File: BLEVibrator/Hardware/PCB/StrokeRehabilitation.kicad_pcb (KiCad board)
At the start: 2 copper layers, 32 x 48 mm, 26 parts, among them CON1 USB-MICRO-B, P2 Programming Header, Q1 MOS_P, Q2 MOSFET_N, SW1 SWITCH_INV, U1 MCP73833, U2 TPS73701_DRV_6, U3 RFD22301, U4 Brushed_DC_motor

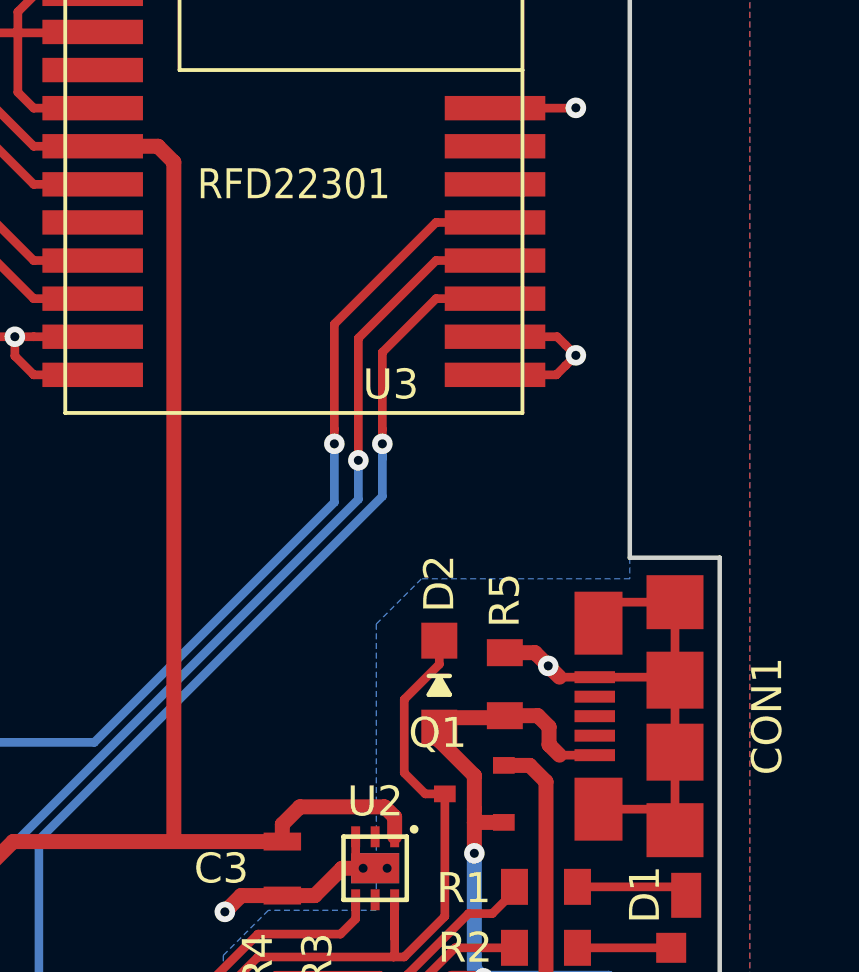
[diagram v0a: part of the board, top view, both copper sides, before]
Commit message: Place and route of LiPo voltage monitoring circuit
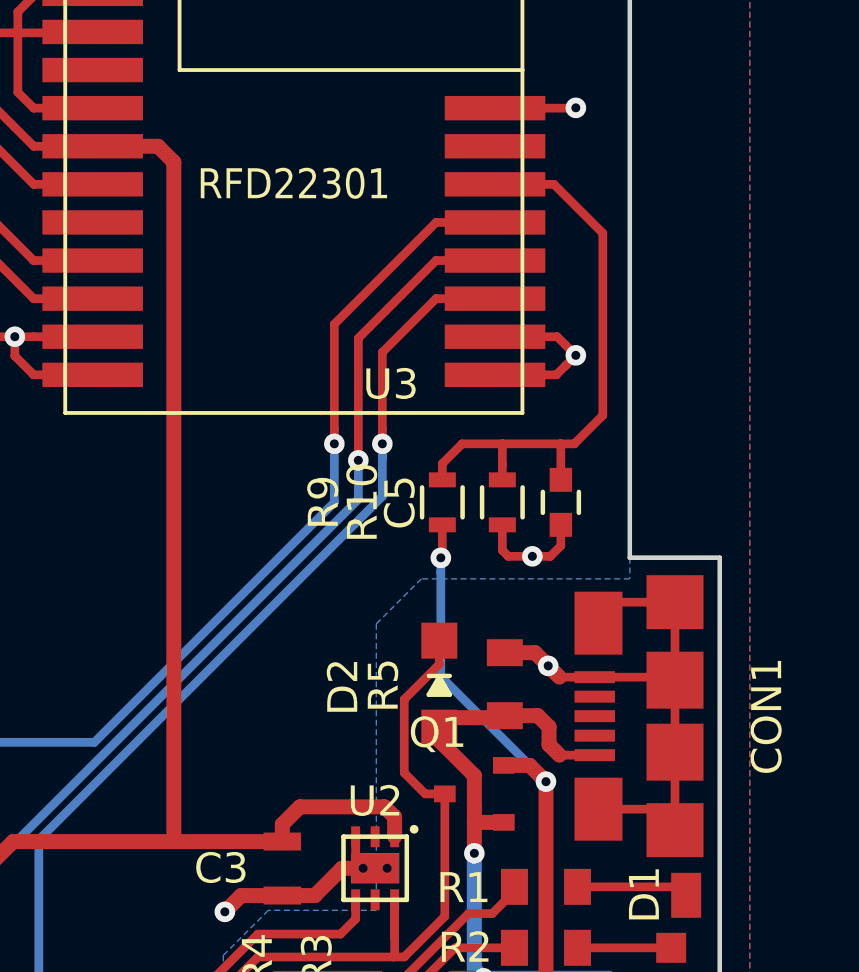
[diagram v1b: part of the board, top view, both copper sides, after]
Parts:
- added C5: 100n, Capacitors_SMD:C_0603, F.Cu at (164.2, 119.9)
- added R10: 2.2M, Resistors_SMD:R_0603, F.Cu at (162.3, 119.9)
- added R9: 10M, Resistors_SMD:R_0603, F.Cu at (160.3, 119.9)
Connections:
- U3 pad P$6: Net-(U3-PadP$6) -> BatteryLevel
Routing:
- net BatteryLevel: track 0.00 -> 19.3 mm
- net +BATT: track 21.6 -> 31.6 mm, vias 0 -> 2
- net GND: track 77.4 -> 81.1 mm, vias 8 -> 9

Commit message: Adding a test point for FACTORY pin of the RFDuino, in case SWD programming is needed in the future
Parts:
- added P1: CONN_01X01, IainPersonalLibrary:TestPoint_SMD_1x1, F.Cu at (140.8, 107.6)
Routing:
- net Net-(P1-Pad1): track 0.00 -> 11.9 mm, vias 0 -> 2
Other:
- net class Default: via_drill 0.3 -> 0.3302
- net class HighCurrent: via_drill 0.3 -> 0.3302
- net class Minimum: via_dia 0.508 -> 0.6858; via_drill 0.3 -> 0.3302
- net class Small: via_drill 0.3 -> 0.3302
- rule via_min_drill: 0.3 -> 0.3302
- rule via_min_size: 0.508 -> 0.6858
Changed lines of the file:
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@@
 (kicad_pcb (version 4) (host pcbnew 4.0.1-stable)
   (general
-    (links 85)
+    (links 86)
     (no_connects 0)
     (area 137.474999 99.424999 169.620601 147.575001)
     (thickness 0.800001)
     (drawings 22)
-    (tracks 293)
+    (tracks 300)
     (zones 0)
-    (modules 29)
+    (modules 30)
     (nets 32)
   )
@@
     (edge_width 0.15)
     (via_size 0.6858)
-    (via_drill 0.3)
-    (via_min_size 0.508)
-    (via_min_drill 0.3)
-    (user_via 0.508 0.3302)
+    (via_drill 0.3302)
+    (via_min_size 0.6858)
+    (via_min_drill 0.3302)
+    (user_via 0.6858 0.3302)
     (uvia_size 0.762)
     (uvia_drill 0.508)
@@
     (pad_drill 0.8)
     (pad_to_mask_clearance 0.2)
-    (aux_axis_origin 128.55 147.5)
-    (grid_origin 128.55 147.5)
+    (aux_axis_origin 137.55 147.5)
+    (grid_origin 137.55 147.5)
     (visible_elements 7FFFFF7F)
     (pcbplotparams
@@
   (net 28 "Net-(U3-PadP$7)")
   (net 29 "Net-(U3-PadP$11)")
-  (net 30 "Net-(U3-PadP$15)")
-  (net 31 BatteryLevel)
+  (net 30 BatteryLevel)
+  (net 31 "Net-(P1-Pad1)")
   (net_class Default "This is the default net class."
     (clearance 0.2)
     (trace_width 0.29)
     (via_dia 0.6858)
-    (via_drill 0.3)
+    (via_drill 0.3302)
     (uvia_dia 0.762)
     (uvia_drill 0.508)
@@
     (add_net "Net-(D3-Pad2)")
     (add_net "Net-(D3-Pad3)")
+    (add_net "Net-(P1-Pad1)")
     (add_net "Net-(P2-Pad2)")
     (add_net "Net-(P2-Pad3)")
@@
     (add_net "Net-(U2-Pad5)")
     (add_net "Net-(U3-PadP$11)")
-    (add_net "Net-(U3-PadP$15)")
     (add_net "Net-(U3-PadP$7)")
     (add_net VDD)
@@
     (trace_width 0.5)
     (via_dia 0.6858)
-    (via_drill 0.3)
+    (via_drill 0.3302)
     (uvia_dia 0.762)
     (uvia_drill 0.508)
@@
     (clearance 0.1524)
     (trace_width 0.1524)
-    (via_dia 0.508)
-    (via_drill 0.3)
+    (via_dia 0.6858)
+    (via_drill 0.3302)
     (uvia_dia 0.762)
     (uvia_drill 0.508)
@@
     (trace_width 0.29)
     (via_dia 0.6858)
-    (via_drill 0.3)
+    (via_drill 0.3302)
     (uvia_dia 0.762)
     (uvia_drill 0.508)
@@
       (net 3 motor) (solder_mask_margin 0.2))
     (pad P$6 smd rect (at -6.7056 0 180) (size 3.3528 0.8128) (layers F.Cu F.Paste F.Mask)
-      (net 31 BatteryLevel) (solder_mask_margin 0.2))
+      (net 30 BatteryLevel) (solder_mask_margin 0.2))
     (pad P$7 smd rect (at -6.7056 1.27 180) (size 3.3528 0.8128) (layers F.Cu F.Paste F.Mask)
       (net 28 "Net-(U3-PadP$7)") (solder_mask_margin 0.2))
@@
       (net 9 "Net-(P2-Pad2)") (solder_mask_margin 0.2))
     (pad P$15 smd rect (at 6.7056 -1.27 180) (size 3.3528 0.8128) (layers F.Cu F.Paste F.Mask)
-      (net 30 "Net-(U3-PadP$15)") (solder_mask_margin 0.2))
+      (net 31 "Net-(P1-Pad1)") (solder_mask_margin 0.2))
     (pad P$16 smd rect (at 6.7056 -2.54 180) (size 3.3528 0.8128) (layers F.Cu F.Paste F.Mask)
       (net 5 "Net-(P2-Pad3)") (solder_mask_margin 0.2))
@@
   (module IainPersonalLibrary:RFDuino_programming_header (layer F.Cu)
     (at 142.85 109.6 270)
-    (fp_text reference P2 (at -0.015 2.048 270) (layer F.SilkS)
+    (fp_text reference P2 (at -1.95 4.15 360) (layer F.SilkS)
       (effects (font (size 1 1) (thickness 0.15)))
     )
@@
     (fp_line (start 0.35 0.6) (end -0.35 0.6) (layer F.SilkS) (width 0.15))
     (pad 1 smd rect (at -0.75 0 270) (size 0.8 0.75) (layers F.Cu F.Paste F.Mask)
-      (net 31 BatteryLevel))
+      (net 30 BatteryLevel))
     (pad 2 smd rect (at 0.75 0 270) (size 0.8 0.75) (layers F.Cu F.Paste F.Mask)
       (net 2 GND))
@@
       (net 10 +BATT))
     (pad 2 smd rect (at 0.75 0 90) (size 0.5 0.9) (layers F.Cu F.Paste F.Mask)
-      (net 31 BatteryLevel))
+      (net 30 BatteryLevel))
     (model Resistors_SMD.3dshapes/R_0603.wrl
       (at (xyz 0 0 0))
@@
     (fp_line (start -0.5 -0.675) (end 0.5 -0.675) (layer F.SilkS) (width 0.15))
     (pad 1 smd rect (at -0.75 0 270) (size 0.5 0.9) (layers F.Cu F.Paste F.Mask)
-      (net 31 BatteryLevel))
+      (net 30 BatteryLevel))
     (pad 2 smd rect (at 0.75 0 270) (size 0.5 0.9) (layers F.Cu F.Paste F.Mask)
       (net 2 GND))
@@
       (rotate (xyz 0 0 0))
     )
+  )
+  (module IainPersonalLibrary:TestPoint_SMD_1x1 (layer F.Cu)
+    (at 140.85 107.6)
+    (fp_text reference P1 (at 2 9.3) (layer F.SilkS)
+      (effects (font (size 1 1) (thickness 0.15)))
+    )
+    (fp_text value CONN_01X01 (at 0.05 -3.6) (layer F.Fab) hide
+      (effects (font (size 1 1) (thickness 0.15)))
+    )
+    (pad 1 smd rect (at 0 0) (size 1.6 1.6) (layers F.Cu F.Mask)
+      (net 31 "Net-(P1-Pad1)"))
   )
   (gr_line (start 166.5484 121.7444) (end 166.5484 99.5) (layer Edge.Cuts) (width 0.15))
@@
   (segment (start 146.85 141.612) (end 146.838 141.624) (width 0.29) (layer F.Cu) (net 24))
   (via (at 146.85 138.55) (size 0.6858) (drill 0.3) (layers F.Cu B.Cu) (net 24))
-  (segment (start 160.96 117.95) (end 162.3 117.95) (width 0.29) (layer F.Cu) (net 31))
-  (segment (start 162.3 117.95) (end 164.25 117.95) (width 0.29) (layer F.Cu) (net 31))
-  (segment (start 162.3 119.15) (end 162.3 118.61) (width 0.29) (layer F.Cu) (net 31))
-  (segment (start 162.3 118.61) (end 162.3 117.95) (width 0.29) (layer F.Cu) (net 31))
-  (segment (start 164.25 117.95) (end 164.7 117.95) (width 0.29) (layer F.Cu) (net 31))
-  (segment (start 164.25 119.15) (end 164.25 117.95) (width 0.29) (layer F.Cu) (net 31))
-  (segment (start 164.7 117.95) (end 165.65 117) (width 0.29) (layer F.Cu) (net 31))
-  (segment (start 165.65 117) (end 165.65 110.928) (width 0.29) (layer F.Cu) (net 31))
-  (segment (start 160.3 119.15) (end 160.3 118.61) (width 0.29) (layer F.Cu) (net 31))
-  (segment (start 160.3 118.61) (end 160.96 117.95) (width 0.29) (layer F.Cu) (net 31))
-  (segment (start 165.65 110.928) (end 164.022 109.3) (width 0.29) (layer F.Cu) (net 31))
-  (segment (start 164.022 109.3) (end 162.0556 109.3) (width 0.29) (layer F.Cu) (net 31))
+  (segment (start 160.96 117.95) (end 162.3 117.95) (width 0.29) (layer F.Cu) (net 30))
+  (segment (start 162.3 117.95) (end 164.25 117.95) (width 0.29) (layer F.Cu) (net 30))
+  (segment (start 162.3 119.15) (end 162.3 118.61) (width 0.29) (layer F.Cu) (net 30))
+  (segment (start 162.3 118.61) (end 162.3 117.95) (width 0.29) (layer F.Cu) (net 30))
+  (segment (start 164.25 117.95) (end 164.7 117.95) (width 0.29) (layer F.Cu) (net 30))
+  (segment (start 164.25 119.15) (end 164.25 117.95) (width 0.29) (layer F.Cu) (net 30))
+  (segment (start 164.7 117.95) (end 165.65 117) (width 0.29) (layer F.Cu) (net 30))
+  (segment (start 165.65 117) (end 165.65 110.928) (width 0.29) (layer F.Cu) (net 30))
+  (segment (start 160.3 119.15) (end 160.3 118.61) (width 0.29) (layer F.Cu) (net 30))
+  (segment (start 160.3 118.61) (end 160.96 117.95) (width 0.29) (layer F.Cu) (net 30))
+  (segment (start 165.65 110.928) (end 164.022 109.3) (width 0.29) (layer F.Cu) (net 30))
+  (segment (start 164.022 109.3) (end 162.0556 109.3) (width 0.29) (layer F.Cu) (net 30))
+  (segment (start 140.85 105.6) (end 140.85 107.6) (width 0.29) (layer F.Cu) (net 31))
+  (segment (start 145.5 109.45) (end 141.65 105.6) (width 0.29) (layer B.Cu) (net 31))
+  (segment (start 141.65 105.6) (end 140.85 105.6) (width 0.29) (layer B.Cu) (net 31))
+  (via (at 140.85 105.6) (size 0.6858) (drill 0.3) (layers F.Cu B.Cu) (net 31))
+  (segment (start 148.6444 110.57) (end 146.62 110.57) (width 0.29) (layer F.Cu) (net 31))
+  (segment (start 146.62 110.57) (end 145.5 109.45) (width 0.29) (layer F.Cu) (net 31))
+  (via (at 145.5 109.45) (size 0.6858) (drill 0.3) (layers F.Cu B.Cu) (net 31))
   (zone (net 2) (net_name GND) (layer B.Cu) (hatch edge 0.508)
     (connect_pads (clearance 0.25))

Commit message: Added back silkscreen with board info
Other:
- board text added: "BLEVibrator v0.3 Designed by Iain Chalmers https://github.com/icchalmers/Sit-To-Stand"
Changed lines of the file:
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@@
     (area 137.474999 99.424999 169.620601 147.575001)
     (thickness 0.800001)
-    (drawings 22)
+    (drawings 23)
     (tracks 300)
     (zones 0)
@@
     (visible_elements 7FFFFF7F)
     (pcbplotparams
-      (layerselection 0x010a8_80000001)
+      (layerselection 0x010f8_80000001)
       (usegerberextensions true)
+      (usegerberattributes true)
       (excludeedgelayer true)
       (linewidth 0.100000)
@@
       (plotinvisibletext false)
       (padsonsilk false)
-      (subtractmaskfromsilk false)
+      (subtractmaskfromsilk true)
       (outputformat 1)
       (mirror false)
@@
       (net 31 "Net-(P1-Pad1)"))
   )
+  (gr_text "BLEVibrator v0.3\nDesigned by Iain Chalmers\nhttps://github.com/icchalmers/Sit-To-Stand" (at 149.65 122.2 90) (layer B.SilkS)
+    (effects (font (size 1 1) (thickness 0.25)) (justify mirror))
+  )
   (gr_line (start 166.5484 121.7444) (end 166.5484 99.5) (layer Edge.Cuts) (width 0.15))
